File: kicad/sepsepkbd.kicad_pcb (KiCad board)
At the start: 2 copper layers, 142.4 x 134.1 mm, 47 parts, among them J1 MJ-4PP-9, J2 Conn_01x04_Socket, J3 Conn_01x04_Socket, SW1 SW_PUSH, SW10 SW_PUSH, SW11 SW_PUSH, SW12 SW_PUSH, SW13 SW_PUSH, SW14 SW_PUSH, SW15 SW_PUSH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

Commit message: add boy's heart
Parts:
- moved SW19 67.7 mm to (208.3, 118.9), turned to -120 degrees
- moved D19 64.8 mm to (199.6, 124.4), turned to 150 degrees
- moved SW20 51.0 mm to (190.9, 105.6), turned to -135 degrees
- moved D20 46.2 mm to (181.3, 108.4), turned to 135 degrees
- moved J1 38.5 mm to (173.8, 40.1), turned to 0 degrees
- moved SW21 35.7 mm to (177.5, 88.2), turned to -150 degrees
- moved J3 30.6 mm to (163.5, 97.7), turned to -150 degrees
- moved SW_RESET1 30.3 mm to (172.9, 60.3), turned to -90 degrees
- moved D21 28.9 mm to (167.4, 88.4), turned to 120 degrees
- moved J2 10.3 mm to (151.4, 76.5), turned to -45 degrees
- moved U1 1.72 mm to (157.9, 56.5)
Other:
- board size 142.4 x 134.1 mm -> 202.9 x 111.3 mm

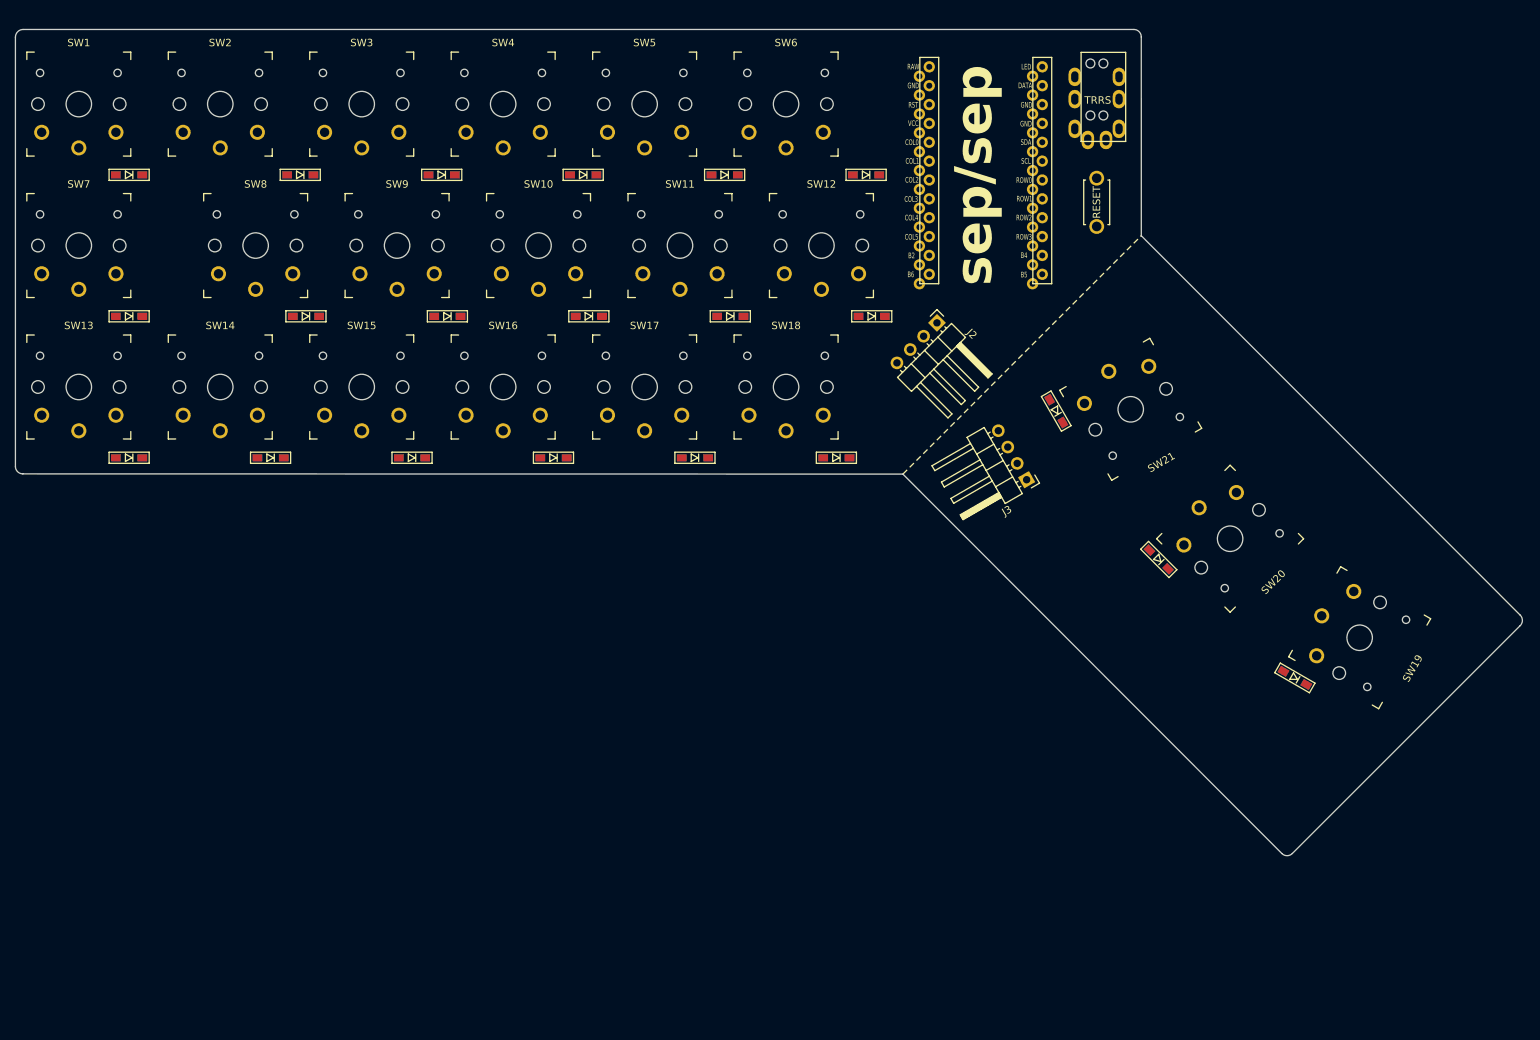
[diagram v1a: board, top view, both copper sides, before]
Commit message: adjust diord position
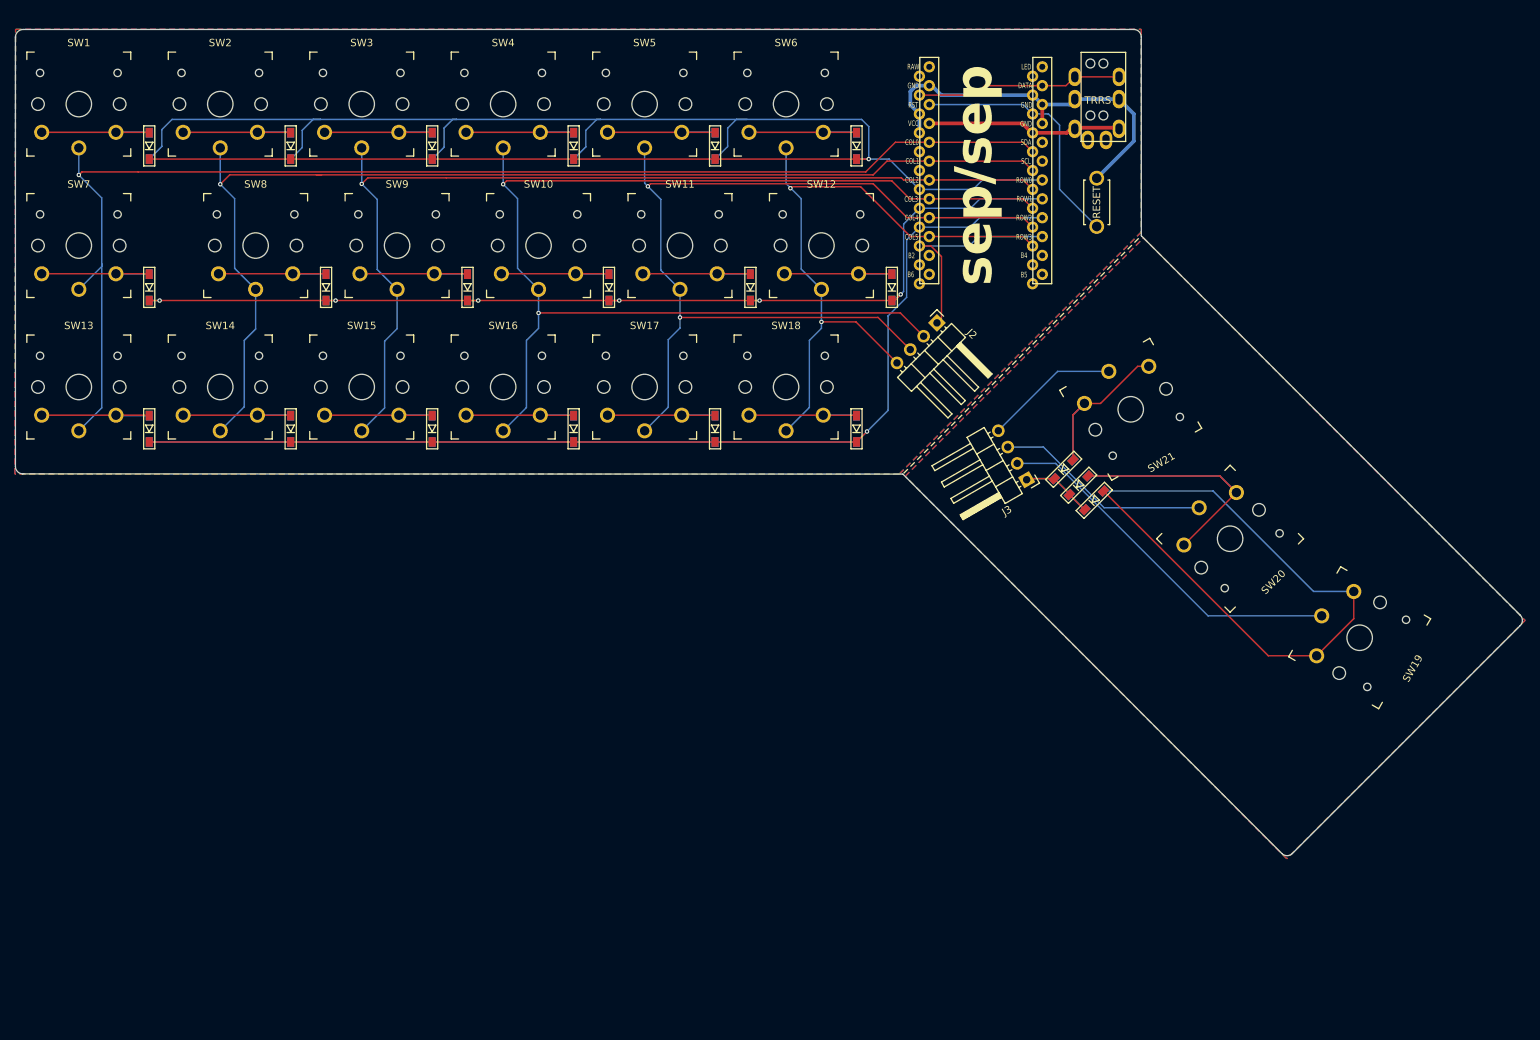
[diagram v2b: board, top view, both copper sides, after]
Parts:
- moved D19 36.1 mm to (172.6, 100.4), turned to 45 degrees
- moved D20 14.7 mm to (170.5, 98.4), turned to 45 degrees
- moved D21 7.90 mm to (168.4, 96.3), turned to 45 degrees
- moved D18 4.75 mm to (140.6, 90.8), turned to 90 degrees
- moved D10 4.75 mm to (107.2, 71.8), turned to 90 degrees
- moved D11 4.75 mm to (126.3, 71.8), turned to 90 degrees
- moved D15 4.75 mm to (83.4, 90.8), turned to 90 degrees
- moved D16 4.75 mm to (102.5, 90.8), turned to 90 degrees
- moved D17 4.75 mm to (121.5, 90.8), turned to 90 degrees
- moved D8 4.75 mm to (69.1, 71.8), turned to 90 degrees
- moved D9 4.75 mm to (88.2, 71.8), turned to 90 degrees
- moved D1 4.75 mm to (45.3, 52.7), turned to 90 degrees
- moved D13 4.75 mm to (45.3, 90.8), turned to 90 degrees
- moved D14 4.75 mm to (64.3, 90.8), turned to 90 degrees
- moved D7 4.75 mm to (45.3, 71.8), turned to 90 degrees
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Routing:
- net row0: track 0.00 -> 259.1 mm, vias 0 -> 1
- net row2: track 0.00 -> 242.0 mm, vias 0 -> 1
- net col0: track 0.00 -> 176.2 mm, vias 0 -> 1
- net col3: track 0.00 -> 168.2 mm, vias 0 -> 2
- net col1: track 0.00 -> 154.0 mm, vias 0 -> 1
- net row1: track 0.00 -> 139.5 mm, vias 0 -> 6
- net col2: track 0.00 -> 133.4 mm, vias 0 -> 1
- net col4: track 0.00 -> 129.2 mm, vias 0 -> 2
- net col5: track 0.00 -> 90.5 mm, vias 0 -> 2
- net Net-(D19-A): track 0.00 -> 87.9 mm
- net GND: track 0.00 -> 51.9 mm
- net Net-(D20-A): track 0.00 -> 51.8 mm
- net Net-(J3-Pin_2): track 0.00 -> 49.5 mm
- net reset: track 0.00 -> 34.4 mm
- net row3: track 0.00 -> 29.8 mm
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- added copper zone on B.Cu, net GND
- added copper zone on F.Cu, net GND
